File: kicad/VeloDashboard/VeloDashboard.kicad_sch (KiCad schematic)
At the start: 47 parts, among them IC1 LDD-700L, IC2 LDD-700L, IC3 LDD-700L, IC4 LDD-700L, IC5 LDD-700L, IC6 LDD-700L, J1 OLED 128 x 64, J1.out1 Polulu Power, J2 Speed Sensor, J3 Conn_01x08_Pin, J4 Conn_01x08_Pin, SW1 On / Off switch, SW2 Left, SW3 Down (lights), SW4 Up (lights), SW5 Brake, SW6 Horn, SW7 Display, SW8 Right, U1 SN74AHCT125N, U2 LC78_05 2.0, U3 Teensy4.0

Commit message: footprints
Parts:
- C1: footprint (none) -> Capacitor_THT:CP_Radial_D10.0mm_P7.50mm
- D1, D2: footprint (none) -> LED_THT:LED_D5.0mm_Clear
- IC1, IC2, IC3, IC4, IC5, IC6: footprint LDD-XXXL -> LDD:LDD-XXXL
- R1, R10, R11, R12, R13, R14, R15, R16, R17, R18, R19, R2, R20, R3, R4, R5, R6, R7, R8, R9: footprint (none) -> Resistor_THT:R_Axial_DIN0207_L6.3mm_D2.5mm_P10.16mm_Horizontal
- SW1, SW2, SW3, SW4, SW5, SW6, SW7, SW8: footprint (none) -> Button_Switch_THT:SW_PUSH-12mm
- U1: footprint digikey-footprints:DIP-14_W3mm -> Package_DIP:DIP-14_W7.62mm_Socket_LongPads
- U3: footprint (none) -> Teensy:Teensy40_SMT

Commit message: rule check
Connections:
- net GND1 is gone; now on net GND: IC1.4 (-VIN), IC2.4 (-VIN), IC3.4 (-VIN), IC4.4 (-VIN), IC5.4 (-VIN), IC6.4 (-VIN)
- net GND: now also J3.8 (Pin_8), U3.32 (GND)
- net ACCU + (11.1 V LiPo): no longer names the net of J1.in1.1 (Pin_1), J1.in1.2 (Pin_2)
- net ACCU -: no longer names the net of J1.in1.3 (Pin_3), J1.in1.4 (Pin_4)
- no-connect marks 43 -> 45
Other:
- note added: "Accu + (12V)"
- note added: "Accu - (GND)"

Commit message: Refacture schematic & raw pcb
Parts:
- removed J2: Speed Sensor, symbol Connector:Conn_01x02_Pin
- removed SW1: On / Off switch, Button_Switch_THT:SW_PUSH-12mm, symbol Switch:SW_Push
- added J2: LED STRIPS, Connector_PinHeader_2.54mm:PinHeader_1x04_P2.54mm_Horizontal, symbol Connector:Conn_01x04_Pin
- added J5: Speed Sensor, Connector_PinHeader_2.54mm:PinHeader_1x03_P2.54mm_Horizontal, symbol Connector:Conn_01x03_Pin
- added J6: Headlights, Connector_PinHeader_2.54mm:PinHeader_1x04_P2.54mm_Horizontal, symbol Connector:Conn_01x04_Pin
- added J7: Rearlights, Connector_PinHeader_2.54mm:PinHeader_1x04_P2.54mm_Horizontal, symbol Connector:Conn_01x04_Pin
- added J8: Blinkers, Connector_PinHeader_2.54mm:PinHeader_1x04_P2.54mm_Horizontal, symbol Connector:Conn_01x04_Pin
- added J9: PowerSwitch, Connector_PinHeader_2.54mm:PinHeader_1x02_P2.54mm_Horizontal, symbol Connector:Conn_01x02_Pin
- BT1: footprint (none) -> Battery:Battery_Panasonic_CR2032-HFN_Horizontal_CircularHoles
- J1: value OLED 128 x 64 -> OLED; footprint (none) -> Connector_PinHeader_2.54mm:PinHeader_1x04_P2.54mm_Horizontal
- J1.in1: footprint (none) -> Connector_PinHeader_2.54mm:PinHeader_1x07_P2.54mm_Horizontal
- J1.out1: footprint (none) -> Connector_PinHeader_2.54mm:PinHeader_1x06_P2.54mm_Horizontal
- J3: value Conn_01x08_Pin -> To Dashboard; footprint (none) -> Connector_PinHeader_2.54mm:PinHeader_1x08_P2.54mm_Horizontal
- J4: value Conn_01x08_Pin -> To Computer; footprint (none) -> Connector_PinHeader_2.54mm:PinHeader_1x08_P2.54mm_Horizontal
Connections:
- net BLINK L is gone; now on net LED BLINK L: IC5.3 (PWMDIM), R19.2
- net +3.3V: now also J5.1 (Pin_1)
- net +5V: now also J2.3 (Pin_3)
- net GND: now also J2.4 (Pin_4), J5.3 (Pin_3)
- net Power meter: now also U3.14 (12_MISO_MQSL); no longer U3.9 (7_RX2_OUT1A)
- net at U3.6 (4_BCLK2): now also J5.2 (Pin_2)
- net LED BLINK L: now reaches U3.8 (6_OUT1D)
- net at J1.out1.5 (Pin_5): now also J9.2 (Pin_2)
- net at J1.out1.6 (Pin_6): now also J9.1 (Pin_1)
- net BLINK L +: no longer names the net of IC5.6 (+VOUT)
- net BLINK L +: now also J8.4 (Pin_4)
- net BLINK L -: no longer names the net of IC5.5 (-VOUT)
- net BLINK L -: now also J8.3 (Pin_3)
- net BLINK R renamed LED BLINK R
- net LED BLINK R: now also U3.9 (7_RX2_OUT1A)
- net BLINK R +: no longer names the net of IC6.6 (+VOUT)
- net BLINK R +: now also J8.2 (Pin_2)
- net BLINK R -: no longer names the net of IC6.5 (-VOUT)
- net BLINK R -: now also J8.1 (Pin_1)
- net BREAK +: no longer names the net of IC4.6 (+VOUT)
- net BREAK +: now also J7.2 (Pin_2)
- net BREAK -: no longer names the net of IC4.5 (-VOUT)
- net BREAK -: now also J7.1 (Pin_1)
- net FRONT LEFT +: no longer names the net of IC1.6 (+VOUT)
- net FRONT LEFT +: now also J6.4 (Pin_4)
- net FRONT LEFT -: no longer names the net of IC1.5 (-VOUT)
- net FRONT LEFT -: now also J6.3 (Pin_3)
- net FRONT RIGHT +: no longer names the net of IC2.6 (+VOUT)
- net FRONT RIGHT +: now also J6.2 (Pin_2)
- net FRONT RIGHT -: no longer names the net of IC2.5 (-VOUT)
- net FRONT RIGHT -: now also J6.1 (Pin_1)
- net LED strip L: no longer names the net of U1.3 (1Y)
- net LED strip L: now also J2.1 (Pin_1)
- net LED strip R: no longer names the net of U1.6 (2Y)
- net LED strip R: now also J2.2 (Pin_2)
- net REAR +: no longer names the net of IC3.6 (+VOUT)
- net REAR +: now also J7.4 (Pin_4)
- net REAR -: no longer names the net of IC3.5 (-VOUT)
- net REAR -: now also J7.3 (Pin_3)
- no-connect marks 45 -> 43
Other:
- moved on the sheet: BT1, D1, D2, J1, J4, R10, R11, R12, R17, R18, R3, R4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

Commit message: Refacture voor uitbreidingen
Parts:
- added J10: Addon 1, Connector_PinHeader_2.54mm:PinHeader_1x03_P2.54mm_Horizontal, symbol Connector:Conn_01x03_Pin
- added J11: Addon 2, Connector_PinHeader_2.54mm:PinHeader_1x03_P2.54mm_Horizontal, symbol Connector:Conn_01x03_Pin
- added J12: extra led strips, Connector_PinHeader_2.54mm:PinHeader_1x04_P2.54mm_Horizontal, symbol Connector:Conn_01x04_Pin
- added R21, R22, R23, R24: 370, Resistor_THT:R_Axial_DIN0207_L6.3mm_D2.5mm_P10.16mm_Horizontal, symbol Device:R
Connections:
- net +3.3V: now also J10.1 (Pin_1), J11.1 (Pin_1)
- net +5V: now also J12.3 (Pin_3)
- net GND: now also U1.10 (3~{OE}), U1.13 (4~{OE}), J10.3 (Pin_3), J11.3 (Pin_3), J12.4 (Pin_4)
- net Power meter: now also U3.25 (18_A4_SDA0); no longer U3.14 (12_MISO_MQSL)
- net at U3.2 (0_RX1_CRX2_CS1): now also U1.9 (3A)
- net Addon 1: now reaches U3.21 (14_A0_TX3_SPDIF_OUT)
- net Addon 1: now also J10.2 (Pin_2)
- net Addon 2: now reaches U3.22 (15_A1_RX3_SPDIF_IN)
- net Addon 2: now also J11.2 (Pin_2)
- net at R5.1: now also U3.26 (19_A5_SCL0); no longer U3.25 (18_A4_SDA0)
- net at R4.1: now also U3.27 (20_A6_TX5_LRCLK1); no longer U3.26 (19_A5_SCL0)
- net at R3.2: now also U3.28 (21_A7_RX5_BCLK1); no longer U3.27 (20_A6_TX5_LRCLK1)
- net at U3.3 (1_TX1_CTX2_MISO1): now also U1.12 (4A)
- net at J2.1 (Pin_1): now also R21.1; no longer U1.3 (1Y)
- net at J2.2 (Pin_2): now also R22.1; no longer U1.6 (2Y)
- net at U1.11 (4Y): now also R24.2
- net at U1.8 (3Y): now also R23.2
- new net: J12.2 (Pin_2), R24.1
- new net: R21.2, U1.3 (1Y)
- new net: R22.2, U1.6 (2Y)
- new net: J12.1 (Pin_1), R23.1
- no-connect marks 43 -> 33
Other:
- moved on the sheet: BT1, J3, R10, R3, R4, R5, R6, R7, R8, R9, U1, U3

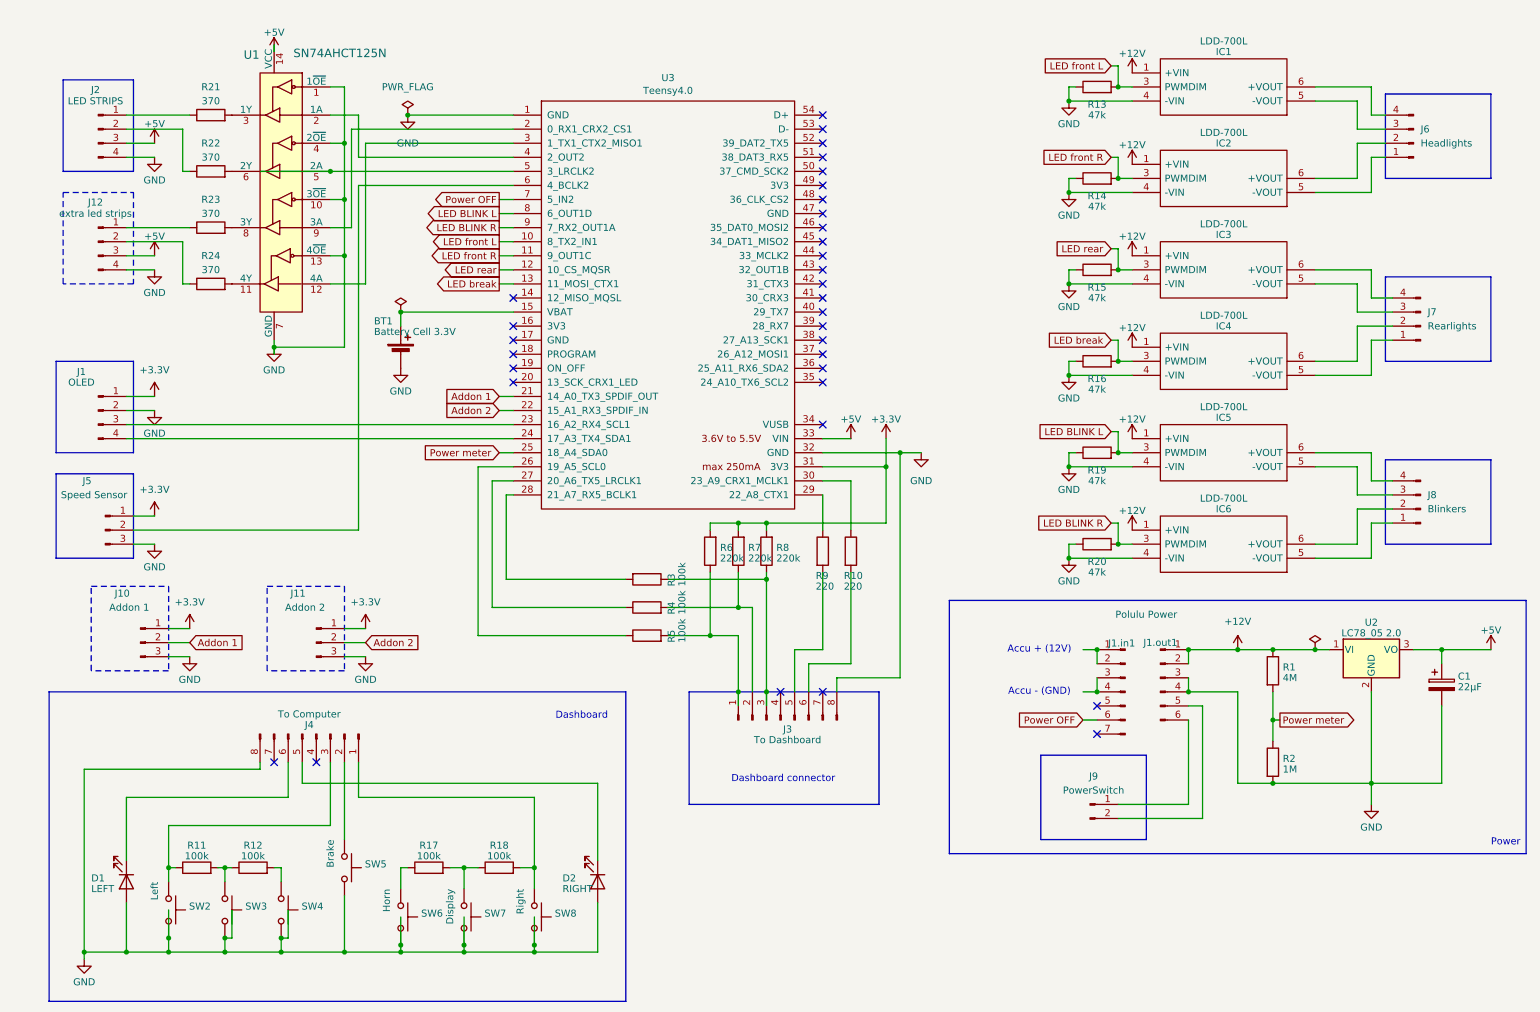
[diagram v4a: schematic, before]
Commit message: rewire dashboard connectors
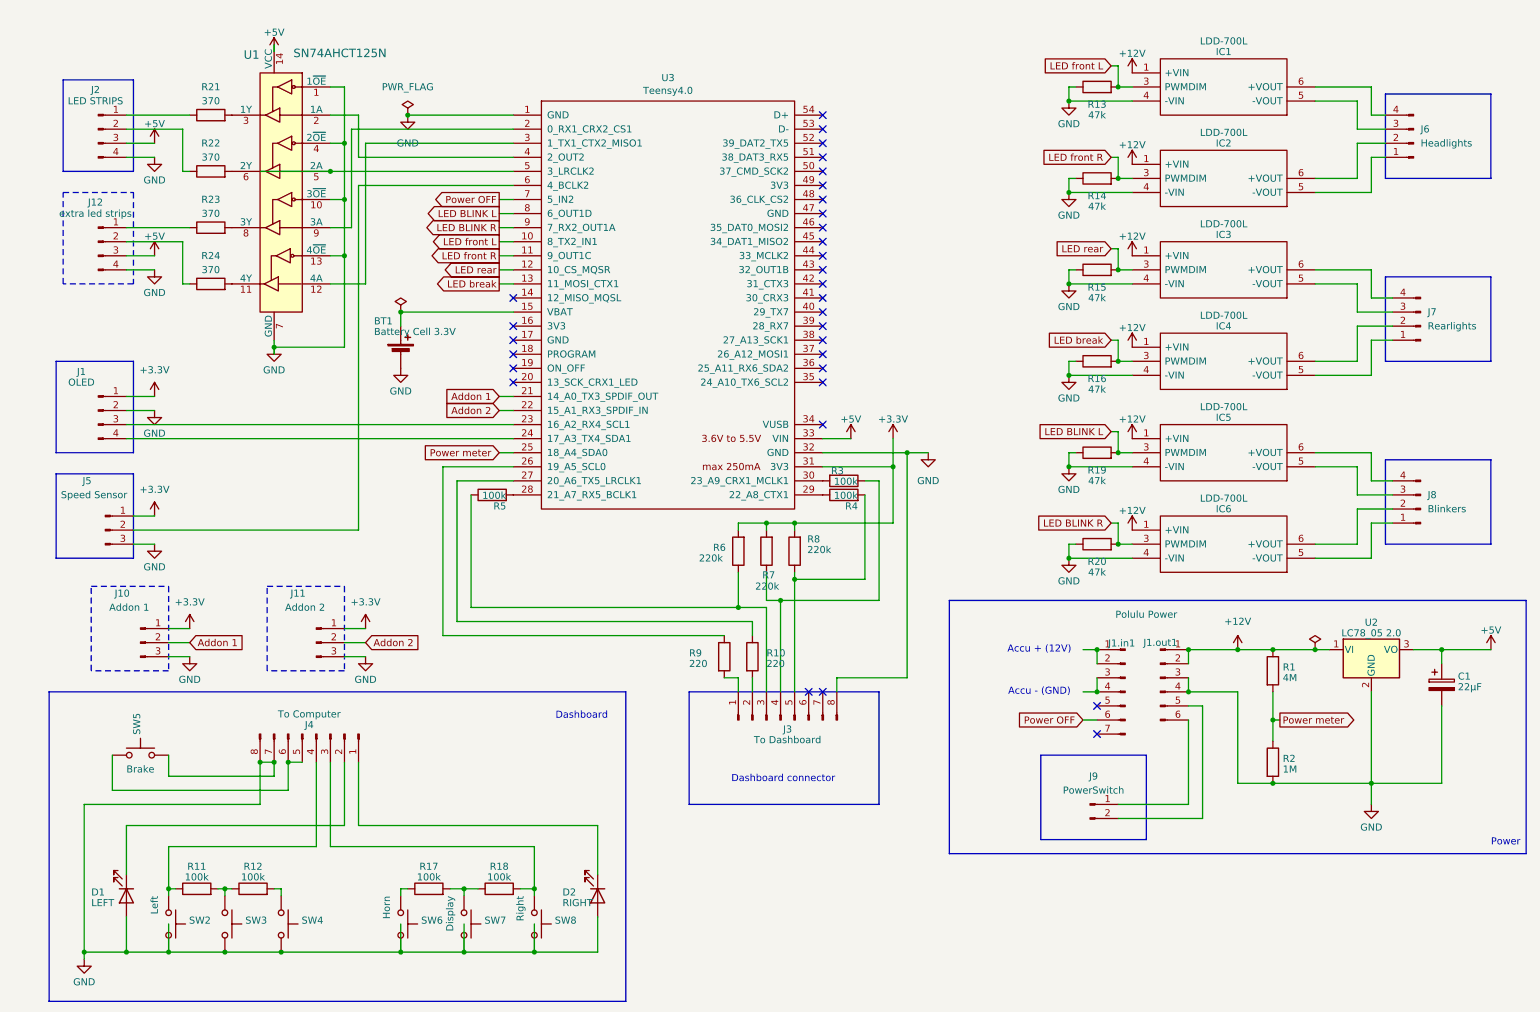
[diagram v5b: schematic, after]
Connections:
- net GND: now also J4.7 (Pin_7)
- net at U3.26 (19_A5_SCL0): now also R9.1; no longer R5.1
- net at U3.27 (20_A6_TX5_LRCLK1): now also R10.1; no longer R4.1
- net at U3.28 (21_A7_RX5_BCLK1): now also R5.2; no longer R3.2
- net at U3.29 (22_A8_CTX1): now also R4.1; no longer R9.1
- net at U3.30 (23_A9_CRX1_MCLK1): now also R3.2; no longer R10.1
- net at D1.1 (K): now also J4.2 (Pin_2); no longer J4.6 (Pin_6)
- net at R10.2: now also J3.2 (Pin_2); no longer J3.6 (Pin_6)
- net at R18.2, SW8.1: now also J4.3 (Pin_3); no longer J4.1 (Pin_1)
- net at D2.1 (K): now also J4.1 (Pin_1); no longer J4.5 (Pin_5)
- net at J3.4 (Pin_4): now also R3.1, R7.1
- net at J3.5 (Pin_5): now also R4.2, R8.1; no longer R9.2
- net at SW5.1: now also J4.5 (Pin_5), J4.6 (Pin_6); no longer J4.2 (Pin_2)
- net at R11.1, SW2.1: now also J4.4 (Pin_4); no longer J4.3 (Pin_3)
- new net: J3.3 (Pin_3), R5.1, R6.1
- new net: J3.1 (Pin_1), R9.2
- no-connect marks 33 -> 31
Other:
- moved on the sheet: D1, D2, R10, R11, R12, R17, R18, R3, R4, R5, R6, R7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

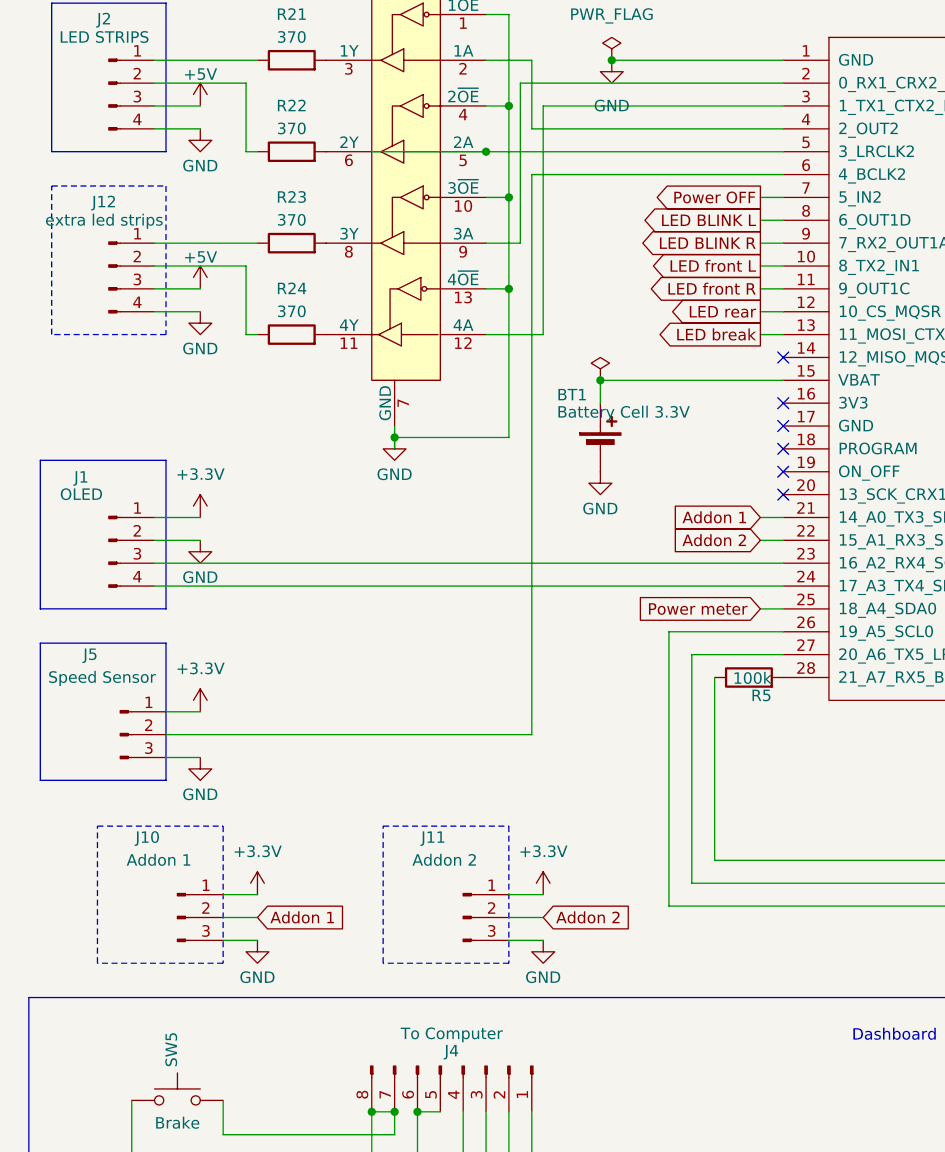
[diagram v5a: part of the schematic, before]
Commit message: refacture due to soldering
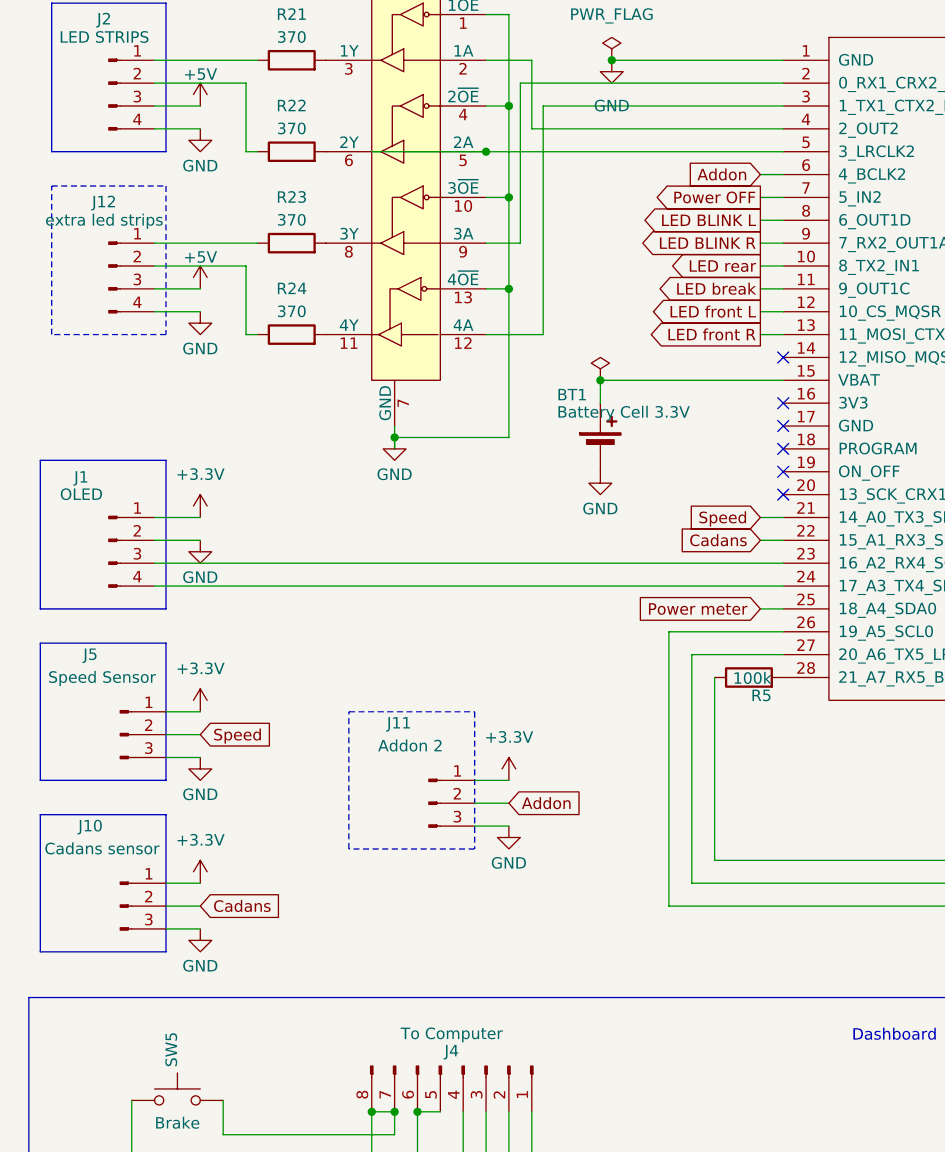
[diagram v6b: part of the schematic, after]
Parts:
- J10: value Addon 1 -> Cadans sensor
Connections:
- net LED break: now also U3.11 (9_OUT1C); no longer U3.13 (11_MOSI_CTX1)
- net LED front L: now also U3.12 (10_CS_MQSR); no longer U3.10 (8_TX2_IN1)
- net LED front R: now also U3.13 (11_MOSI_CTX1); no longer U3.11 (9_OUT1C)
- net LED rear: now also U3.10 (8_TX2_IN1); no longer U3.12 (10_CS_MQSR)
- net Addon: now reaches U3.6 (4_BCLK2)
- net Addon: now also J11.2 (Pin_2); no longer J5.2 (Pin_2)
- net Addon 1 renamed Cadans
- net Cadans: now also U3.22 (15_A1_RX3_SPDIF_IN); no longer U3.21 (14_A0_TX3_SPDIF_OUT)
- removed net Addon 2: J11.2 (Pin_2), U3.22 (15_A1_RX3_SPDIF_IN)
- new net Speed: J5.2 (Pin_2), U3.21 (14_A0_TX3_SPDIF_OUT)
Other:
- company: (none) -> Jan den Besten
- title: (none) -> VeloDashboard
- moved on the sheet: J10, J11
